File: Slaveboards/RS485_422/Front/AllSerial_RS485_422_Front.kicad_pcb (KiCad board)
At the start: 2 copper layers, 71.5 x 24 mm, 3 parts

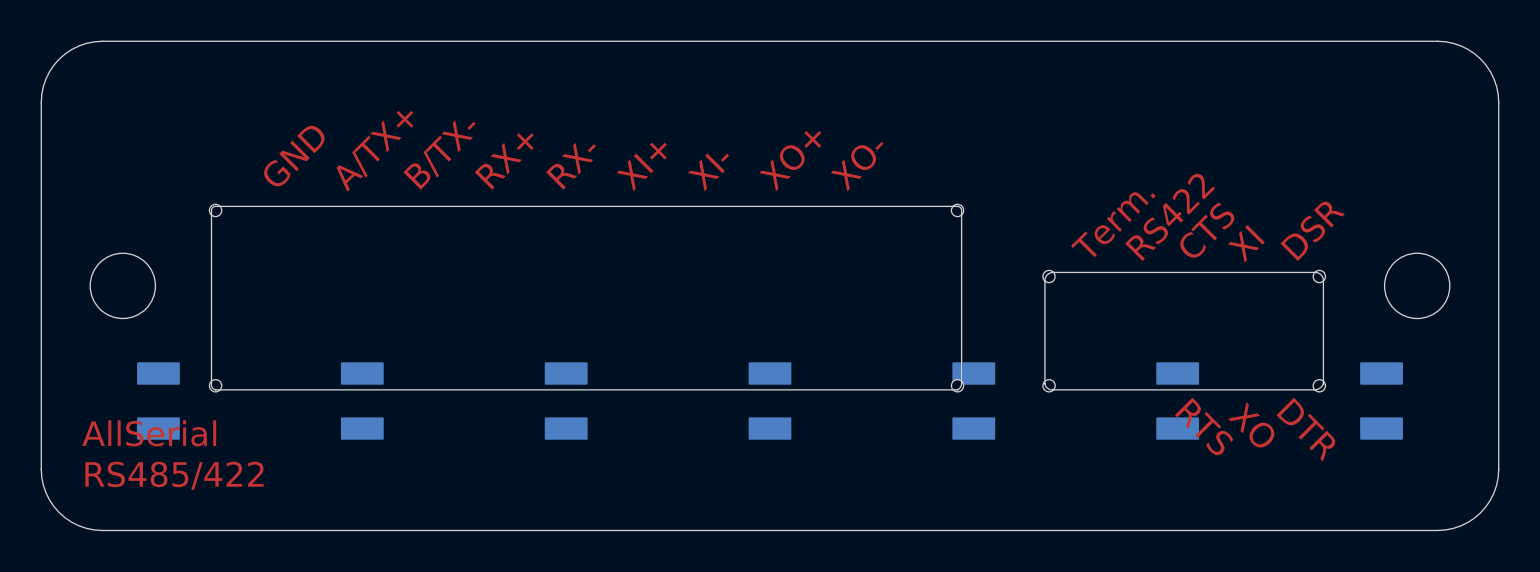
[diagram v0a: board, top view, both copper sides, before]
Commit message: Update AllSerial libraries
update projects
add slave project template
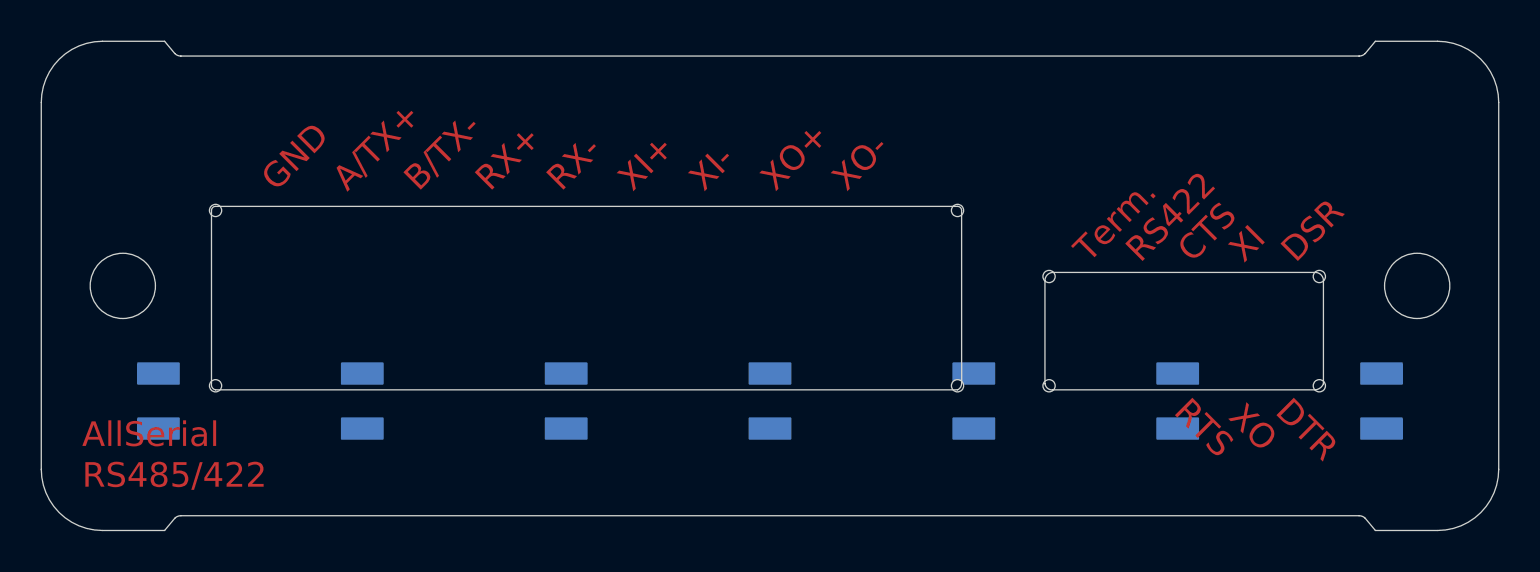
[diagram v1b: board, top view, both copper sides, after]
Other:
- outline, holes or cut-outs redrawn

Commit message: Improve libraries
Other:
- outline, holes or cut-outs redrawn
- board text added: "JLCJLCJLCJLC"

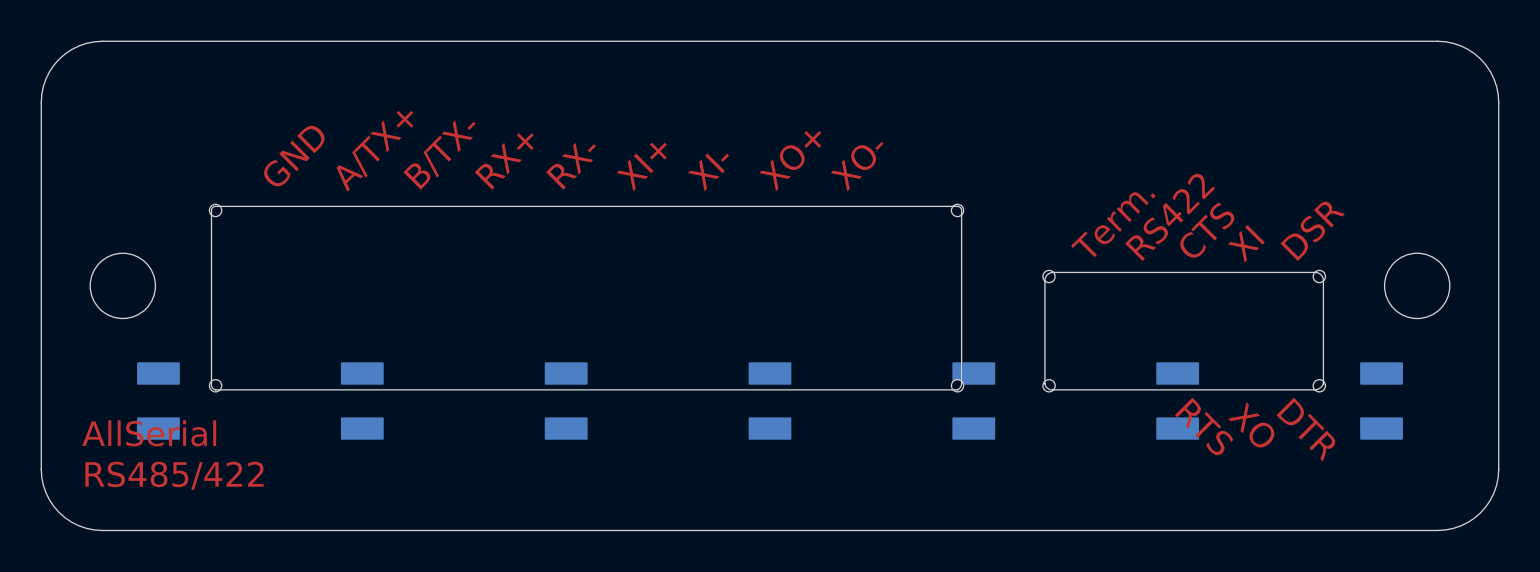
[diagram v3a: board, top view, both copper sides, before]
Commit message: Remove pads from cutouts
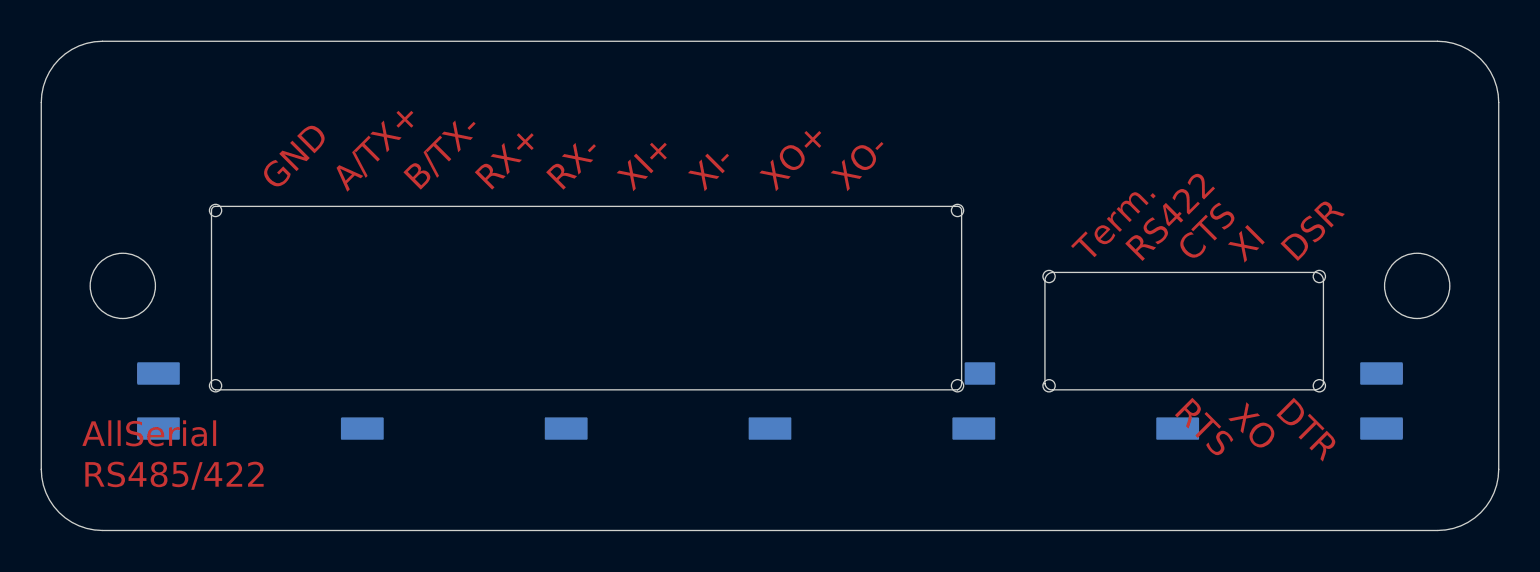
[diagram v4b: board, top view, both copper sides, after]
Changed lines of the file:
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@@
-		)
-		(fp_rect
-			(start -21 -8.2)
-			(end -19 -7.2)
-			(stroke
-				(width 0.1)
-				(type solid)
-			)
-			(fill yes)
-			(layer "B.Cu")
 		)
 		(fp_rect
 			(start -21 -5.5)
 			(end -19 -4.5)
-			(stroke
-				(width 0.1)
-				(type solid)
-			)
-			(fill yes)
-			(layer "B.Cu")
-		)
-		(fp_rect
-			(start -11 -8.2)
-			(end -9 -7.2)
 			(stroke
 				(width 0.1)
@@
 		)
 		(fp_rect
-			(start -1 -8.2)
-			(end 1 -7.2)
-			(stroke
-				(width 0.1)
-				(type solid)
-			)
-			(fill yes)
-			(layer "B.Cu")
-		)
-		(fp_rect
 			(start -1 -5.5)
 			(end 1 -4.5)
-			(stroke
-				(width 0.1)
-				(type solid)
-			)
-			(fill yes)
-			(layer "B.Cu")
-		)
-		(fp_rect
-			(start 9 -8.2)
-			(end 11 -7.2)
 			(stroke
 				(width 0.1)
@@
 		)
 		(fp_rect
-			(start 19 -8.2)
-			(end 21 -7.2)
+			(start 9.6 -8.2)
+			(end 11 -7.2)
 			(stroke
 				(width 0.1)
@@
 		)
 		(fp_rect
-			(start -21 -8.2)
+			(start -21 -5.55)
 			(end -19 -4.5)
 			(stroke
@@
 		)
 		(fp_rect
-			(start -11 -8.2)
+			(start -11 -5.6)
 			(end -9 -4.5)
 			(stroke
@@
 		)
 		(fp_rect
-			(start -1 -8.2)
+			(start -1 -5.55)
 			(end 1 -4.5)
 			(stroke
@@
 		)
 		(fp_rect
-			(start 9 -8.2)
+			(start 9 -5.55)
 			(end 11 -4.5)
 			(stroke
@@
 		)
 		(fp_rect
-			(start 19 -8.2)
+			(start 9.6 -8.2)
+			(end 11 -6.8)
+			(stroke
+				(width 0.1)
+				(type solid)
+			)
+			(fill yes)
+			(layer "B.Mask")
+		)
+		(fp_rect
+			(start 19 -5.6)
 			(end 21 -4.5)
 			(stroke

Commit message: Add python testskript
Add mainboard tester
Add libraries
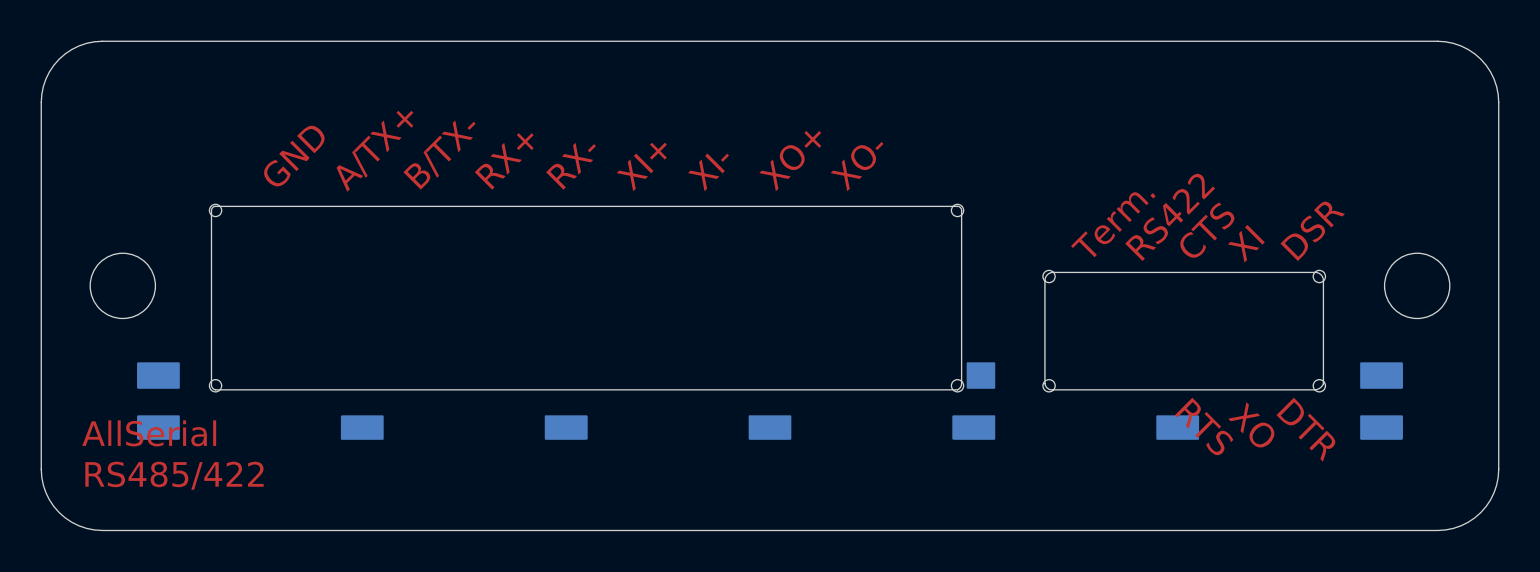
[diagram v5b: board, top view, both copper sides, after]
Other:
- board text removed: "JLCJLCJLCJLC"
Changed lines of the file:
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@@
 		(fp_rect
 			(start -31 -8.2)
-			(end -29 -7.2)
+			(end -29 -7)
 			(stroke
 				(width 0.1)
@@
 		)
 		(fp_rect
-			(start -31 -5.5)
+			(start -31 -5.6)
 			(end -29 -4.5)
 			(stroke
@@
 		)
 		(fp_rect
-			(start -21 -5.5)
+			(start -21 -5.6)
 			(end -19 -4.5)
 			(stroke
@@
 		)
 		(fp_rect
-			(start -11 -5.5)
+			(start -11 -5.6)
 			(end -9 -4.5)
 			(stroke
@@
 		)
 		(fp_rect
-			(start -1 -5.5)
+			(start -1 -5.6)
 			(end 1 -4.5)
 			(stroke
@@
 		)
 		(fp_rect
-			(start 9 -5.5)
+			(start 9 -5.6)
 			(end 11 -4.5)
 			(stroke
@@
 		)
 		(fp_rect
-			(start 9.6 -8.2)
-			(end 11 -7.2)
+			(start 9.7 -8.2)
+			(end 11 -7)
 			(stroke
 				(width 0.1)
@@
 		)
 		(fp_rect
-			(start 19 -5.5)
+			(start 19 -5.6)
 			(end 21 -4.5)
 			(stroke
@@
 		(fp_rect
 			(start 29 -8.2)
-			(end 31 -7.2)
+			(end 31 -7)
 			(stroke
 				(width 0.1)
@@
 		)
 		(fp_rect
-			(start 29 -5.5)
+			(start 29 -5.6)
 			(end 31 -4.5)
 			(stroke
@@
 		)
 		(fp_rect
-			(start -21 -5.55)
+			(start -21 -8.2)
 			(end -19 -4.5)
 			(stroke
@@
 		)
 		(fp_rect
-			(start -11 -5.6)
+			(start -11 -8.2)
 			(end -9 -4.5)
 			(stroke
@@
 		)
 		(fp_rect
-			(start -1 -5.55)
+			(start -1 -8.2)
 			(end 1 -4.5)
 			(stroke
@@
 		)
 		(fp_rect
-			(start 9 -5.55)
+			(start 9 -8.2)
 			(end 11 -4.5)
 			(stroke
@@
 		)
 		(fp_rect
-			(start 9.6 -8.2)
-			(end 11 -6.8)
-			(stroke
-				(width 0.1)
-				(type solid)
-			)
-			(fill yes)
-			(layer "B.Mask")
-		)
-		(fp_rect
-			(start 19 -5.6)
+			(start 19 -8.2)
 			(end 21 -4.5)
 			(stroke
@@
 	)
 	(gr_text "AllSerial RS485/422 v1.5 25/23\nSeegel Systeme"
-		(at 148.5 97.55 0)
+		(at 148.6011 99.6036 0)
 		(layer "B.SilkS")
 		(effects
@@
 		)
 	)
-	(gr_text "JLCJLCJLCJLC"
-		(at 153.5011 115.4036 0)
-		(layer "B.SilkS")
-		(effects
-			(font
-				(size 1 1)
-				(thickness 0.15)
-			)
-			(justify left bottom mirror)
-		)
-	)
